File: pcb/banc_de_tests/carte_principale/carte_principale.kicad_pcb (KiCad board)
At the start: 2 copper layers, 54.5 x 50 mm, 40 parts, among them J1 Arduino_UNO_R3, J2 Conn_02x10_Odd_Even, J3 Conn_01x02, U1 AMS1117-3.3, U2 TSV911AILT, U4 74LVC2G17, U5 74LVC2G17, U6 74LVC2G17, U7 74LVC2G17

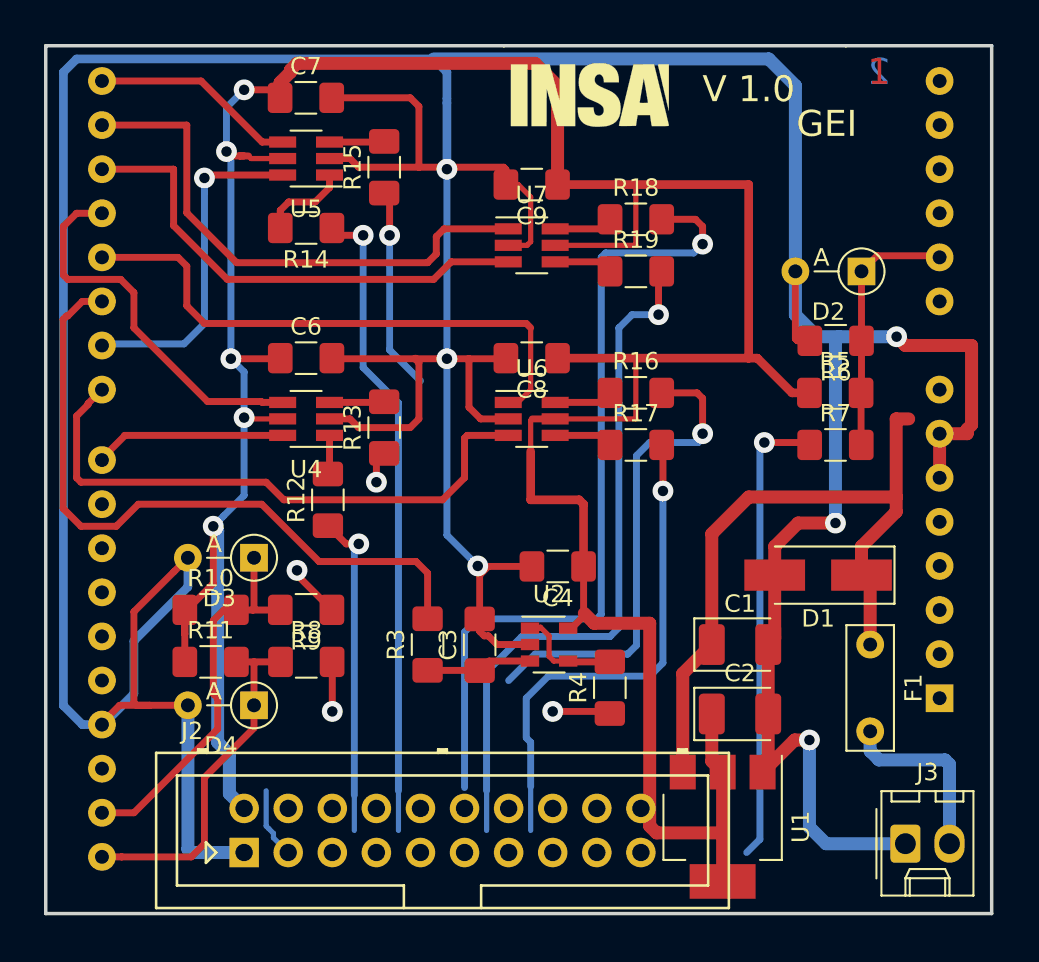
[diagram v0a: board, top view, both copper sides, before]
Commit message: Ajout du bus SPI
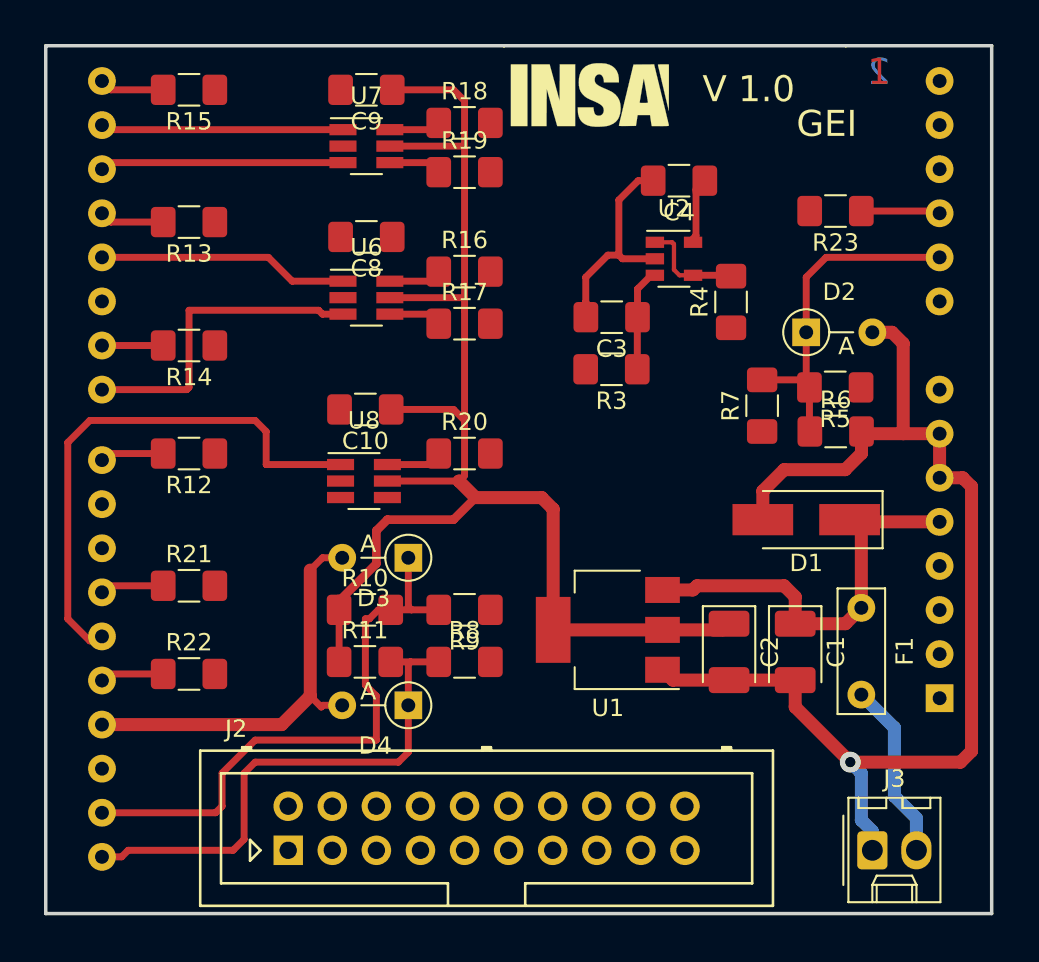
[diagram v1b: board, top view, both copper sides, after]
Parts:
- removed C6, C7: 100nF, Capacitor_SMD:C_1206_3216Metric_Pad1.42x1.75mm_HandSolder
- removed U4, U5: 74LVC2G17, Package_TO_SOT_SMD:SOT-23-6_Handsoldering
- added C10: 100nF, Capacitor_SMD:C_1206_3216Metric_Pad1.42x1.75mm_HandSolder, F.Cu at (108.4, 85.0)
- added R20: 330, Resistor_SMD:R_1206_3216Metric_Pad1.42x1.75mm_HandSolder, F.Cu at (114.1, 87.5)
- added R21: 330, Resistor_SMD:R_1206_3216Metric_Pad1.42x1.75mm_HandSolder, F.Cu at (98.3, 95.1)
- added R22: 330, Resistor_SMD:R_1206_3216Metric_Pad1.42x1.75mm_HandSolder, F.Cu at (98.3, 100.2)
- added R23: 330, Resistor_SMD:R_1206_3216Metric_Pad1.42x1.75mm_HandSolder, F.Cu at (135.5, 73.5)
- added U8: 74LVC2G17, Package_TO_SOT_SMD:SOT-23-6_Handsoldering, F.Cu at (108.3, 89.1)
- moved U2 23.4 mm to (126.2, 76.3)
- moved R4 23.3 mm to (129.5, 78.8)
- moved C4 23.3 mm to (126.5, 71.8)
- moved C3 20.3 mm to (122.6, 79.6), turned to 180 degrees
- moved R3 19.1 mm to (122.6, 82.6), turned to 180 degrees
- moved R13 16.3 mm to (98.3, 74.2), turned to 180 degrees
- moved U1 13.1 mm to (122.4, 97.7), turned to 180 degrees
- moved R15 12.1 mm to (98.3, 66.5), turned to 180 degrees
- moved R16 12.1 mm to (114.1, 77.0)
- moved R17 12.1 mm to (114.1, 80.0)
- moved C8 11.8 mm to (108.5, 75.0)
- moved U6 11.8 mm to (108.5, 78.5)
- moved R19 11.4 mm to (114.1, 71.3)
- moved R18 11.3 mm to (114.1, 68.4)
- moved U7 11.1 mm to (108.5, 69.8)
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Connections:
- J1 pad 11: (no net) -> /SIM_SPI_CS
- J1 pad 26: (no net) -> /SIM_SPI_MOSI
- J1 pad 27: (no net) -> /SIM_SPI_MISO
- J1 pad 28: (no net) -> /SIM_SPI_SCK
- J2 pad 10: /XBEE_UART_RX -> /CAPTEURS_SDA
- J2 pad 11: /GIRO_PHA -> /SPI_MISO
- J2 pad 13: /CARD_DETECT -> /GIRO_PHA
- J2 pad 14: /TENSION_BATTERIE -> /GIRO_INDEX
- J2 pad 15: (no net) -> /XBEE_UART_RX
- J2 pad 16: (no net) -> /TENSION_BATTERIE
- J2 pad 17: (no net) -> /CARD_DETECT
- J2 pad 18: (no net) -> /SPI_CS
- J2 pad 3: /CAPTEURS_SDA -> /SPI_SCK
- J2 pad 4: /CAPTEURS_SCL -> /SPI_MOSI
- J2 pad 6: /MOT_PWM -> /SERVO_PWM
- J2 pad 7: /SERVO_PWM -> /MOT_PWM
- J2 pad 9: /GIRO_INDEX -> /CAPTEURS_SCL
- R12 pad 2: Net-(R12-Pad2) -> /SIM_MOT_DIR
- R13 pad 2: Net-(R13-Pad2) -> /SIM_MOT_PWM
- R14 pad 2: Net-(R14-Pad2) -> /SIM_SERVO_PWM
- R15 pad 2: Net-(R15-Pad2) -> /SIM_UART_TX
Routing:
- net GND: track 293.2 -> 104.4 mm, vias 6 -> 1
- net +3V3: track 188.2 -> 86.0 mm, vias 5 -> 0
- net /XBEE_UART_RX: track 47.5 -> 0.00 mm, vias 1 -> 0
- net /GIRO_INDEX: track 40.3 -> 0.00 mm, vias 1 -> 0
- net /SIM_V_BATTERIE: track 39.8 -> 0.00 mm
- net /SERVO_PWM: track 37.1 -> 0.00 mm, vias 1 -> 0
- net /SIM_SPI_MISO: track 0.00 -> 31.2 mm
- net /GIRO_PHA: track 29.0 -> 0.00 mm, vias 1 -> 0
- net /GIRO_PHB: track 28.1 -> 0.00 mm, vias 1 -> 0
- net /CARD_DETECT: track 26.7 -> 0.00 mm, vias 1 -> 0
- net /MOT_DIR: track 18.8 -> 0.00 mm, vias 1 -> 0
- net /SIM_MOT_PWM: track 22.3 -> 3.74 mm
- net /SIM_GIRO_PHB: track 32.9 -> 14.5 mm
- net /SIM_UART_RX: track 31.1 -> 14.0 mm
- net +5V: track 40.7 -> 24.3 mm
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
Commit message: * Reorganisation du connecteur de la carte etudiant * premiere version de la carte principale du banc de test * premiere version de la carte vers le connecteur de la carte etudiant
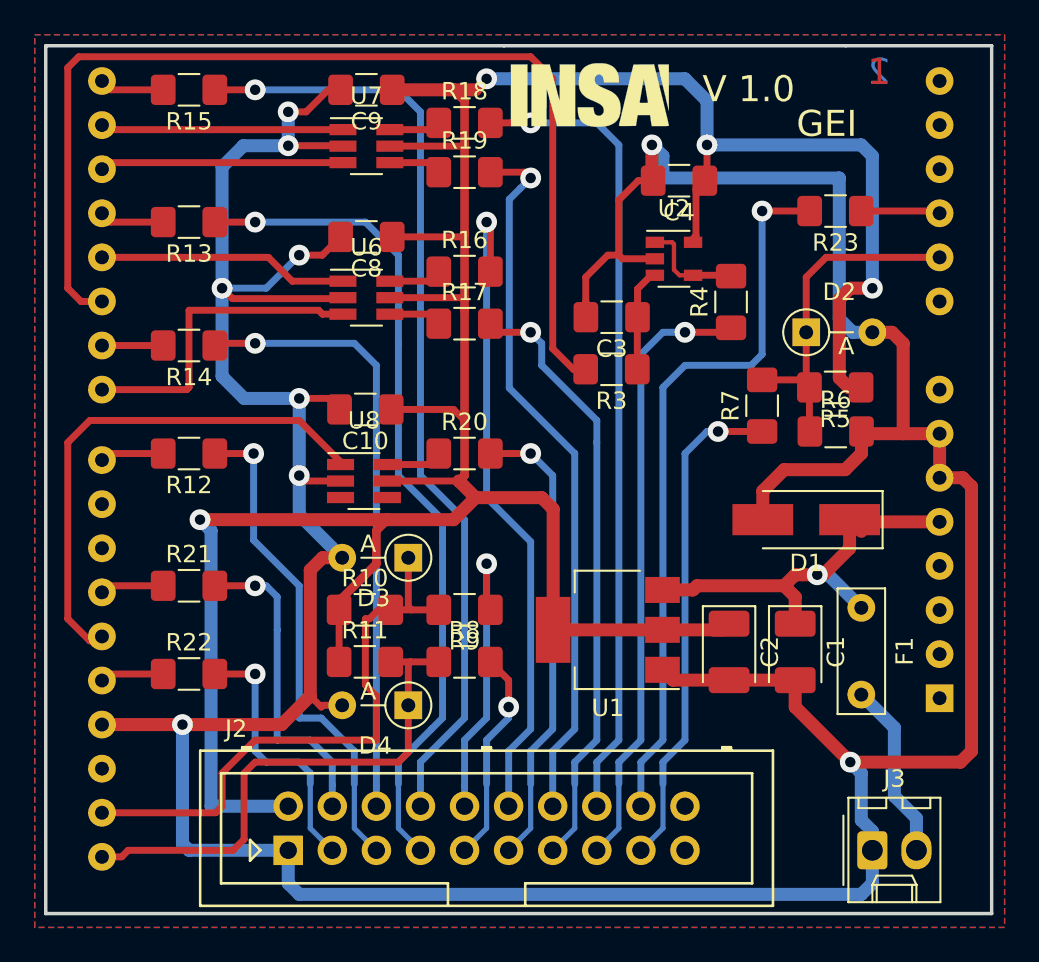
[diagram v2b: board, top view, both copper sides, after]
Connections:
- J2 pad 15: /XBEE_UART_RX -> /TENSION_BATTERIE
- J2 pad 16: /TENSION_BATTERIE -> /XBEE_UART_RX
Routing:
- net GND: track 104.4 -> 240.9 mm, vias 1 -> 9
- net +3V3: track 86.0 -> 167.9 mm, vias 0 -> 4
- net /SIM_V_BATTERIE: track 0.00 -> 61.7 mm
- net /XBEE_UART_TX: track 0.00 -> 54.5 mm, vias 0 -> 1
- net /MOT_PWM: track 0.00 -> 48.3 mm, vias 0 -> 1
- net /XBEE_UART_RX: track 0.00 -> 46.6 mm, vias 0 -> 1
- net /SPI_CS: track 0.00 -> 42.2 mm, vias 0 -> 1
- net /GIRO_INDEX: track 0.00 -> 41.3 mm, vias 0 -> 1
- net /GIRO_PHB: track 0.00 -> 38.2 mm, vias 0 -> 1
- net /TENSION_BATTERIE: track 0.00 -> 35.5 mm, vias 0 -> 1
- net /SERVO_PWM: track 0.00 -> 35.3 mm, vias 0 -> 1
- net /GIRO_PHA: track 0.00 -> 35.0 mm, vias 0 -> 1
- net /CARD_DETECT: track 0.00 -> 28.9 mm, vias 0 -> 1
- net /MOT_DIR: track 0.00 -> 28.8 mm, vias 0 -> 1
- net /SPI_MISO: track 0.00 -> 26.8 mm, vias 0 -> 1
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- added copper zone on B.Cu, net GND
- added copper zone on F.Cu, net GND
